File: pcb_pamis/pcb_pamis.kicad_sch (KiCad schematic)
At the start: 8 parts, among them J1 1755736, J2 USB_A, SW1 SW_Push, U1 ESP32-WROOM-32UE

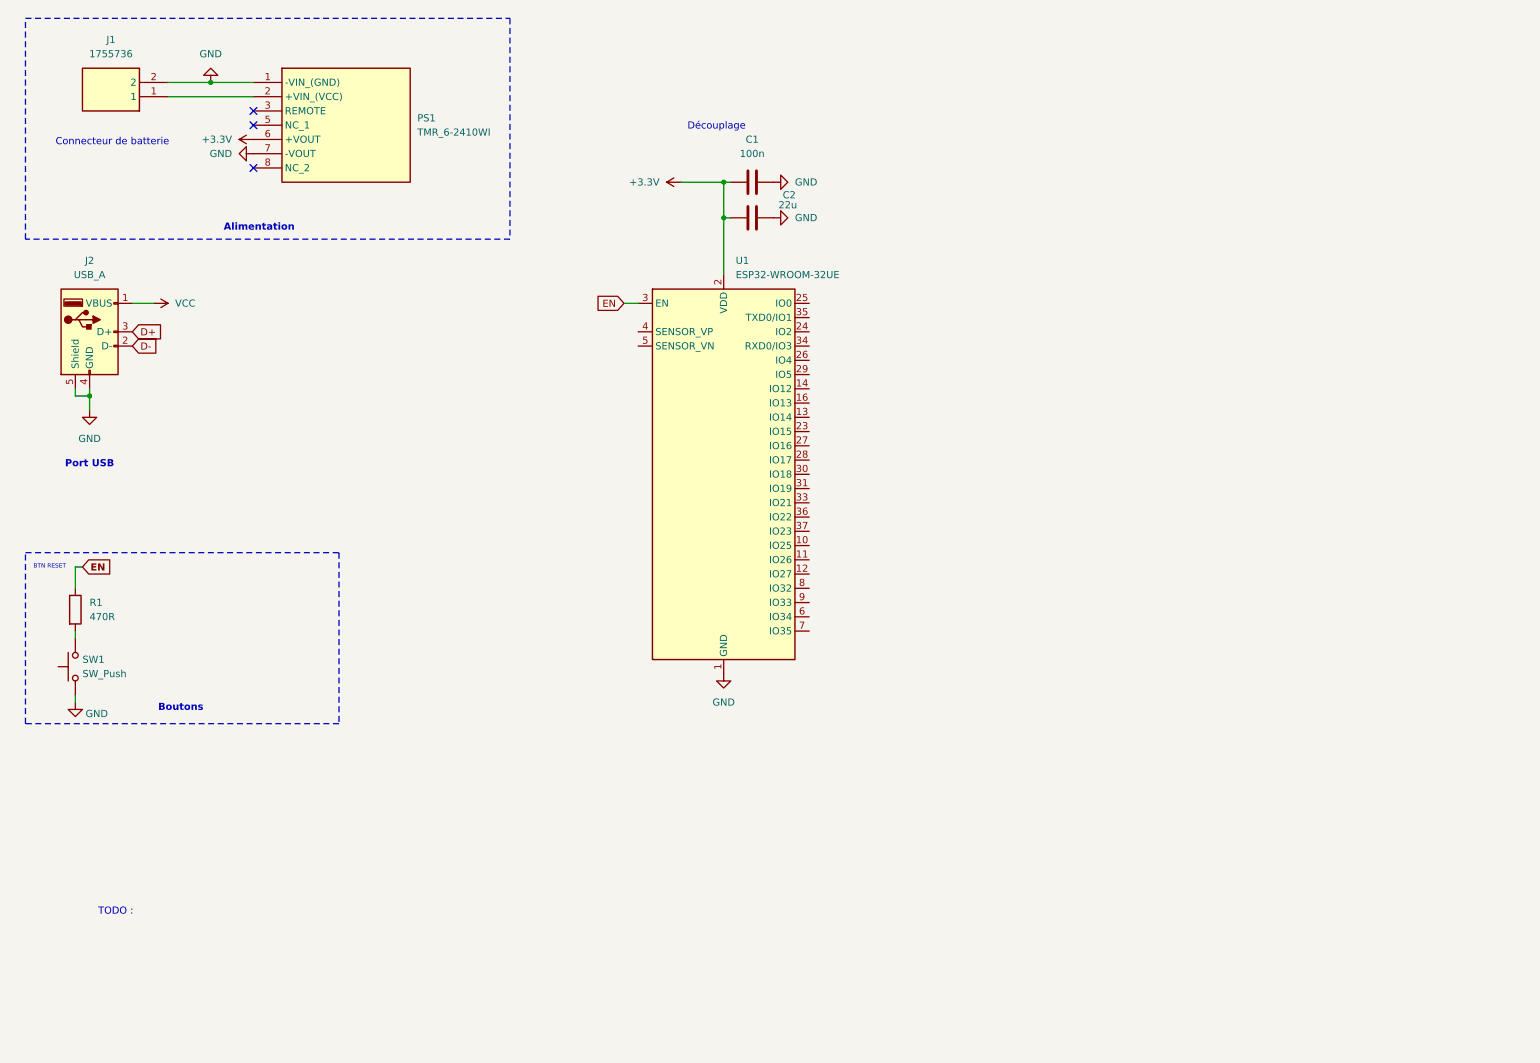
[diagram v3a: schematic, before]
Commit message: feat: add cp2102 usb to uart + auto flash circuit
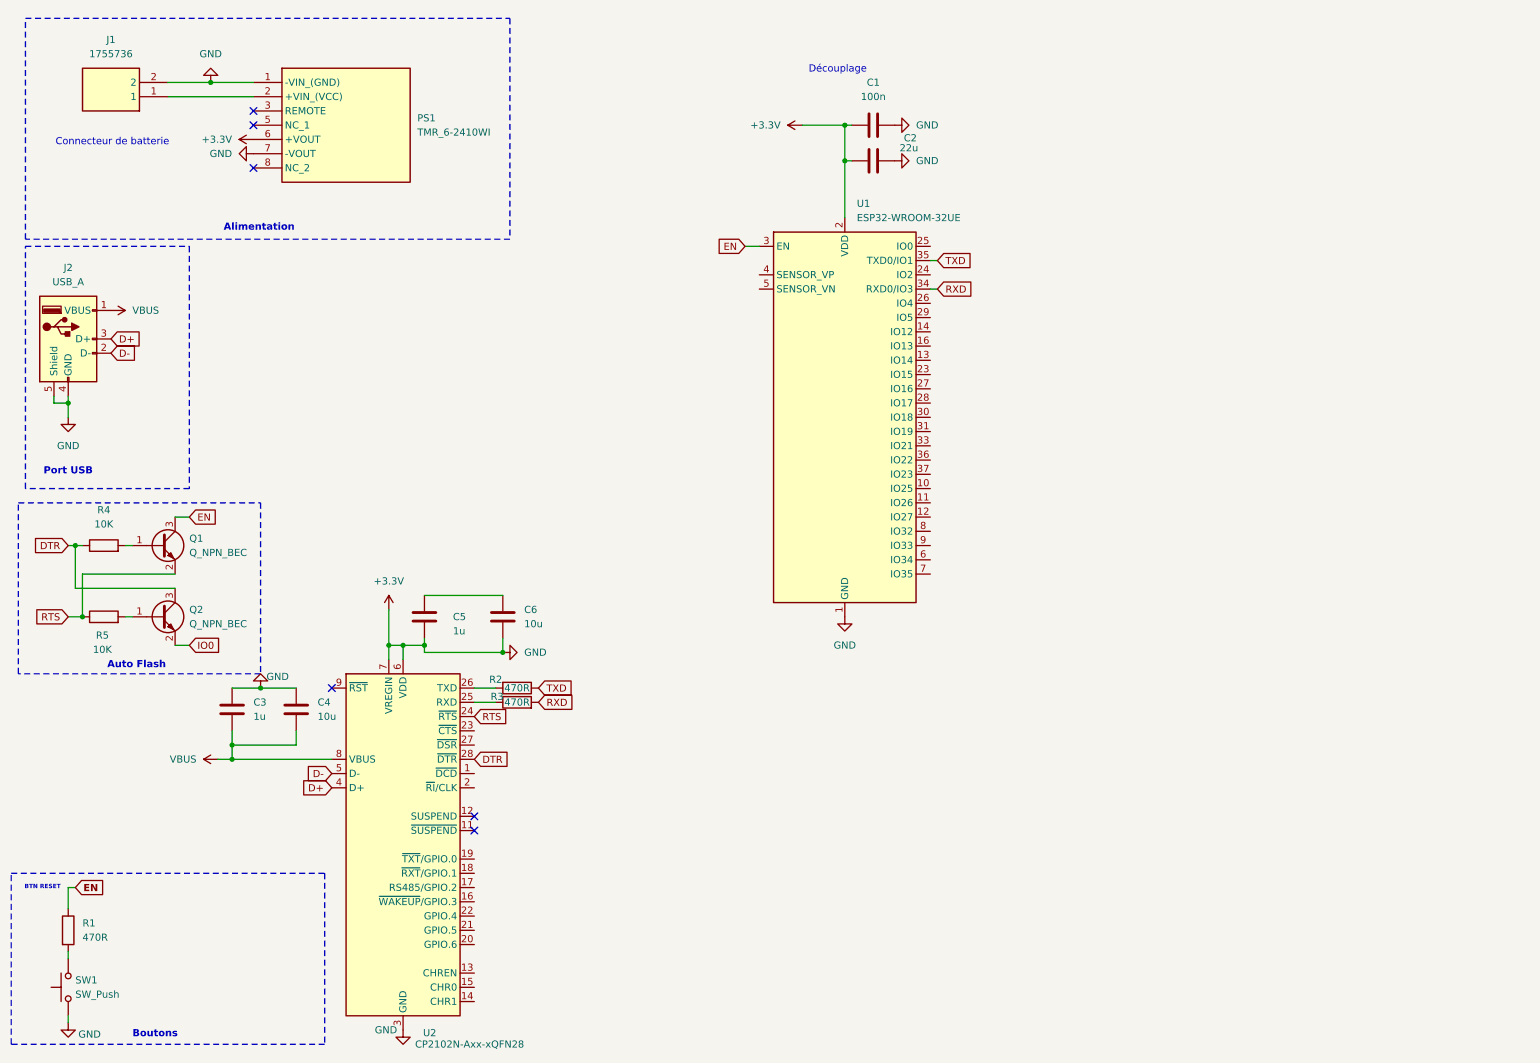
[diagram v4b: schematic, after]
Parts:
- added C3, C5: 1u, Capacitor_SMD:C_0805_2012Metric_Pad1.18x1.45mm_HandSolder, symbol Device:C
- added C4, C6: 10u, Capacitor_SMD:C_0805_2012Metric_Pad1.18x1.45mm_HandSolder, symbol Device:C
- added Q1, Q2: Q_NPN_BEC, symbol Transistor_BJT:Q_NPN_BEC
- added R2, R3: 470R, symbol Device:R
- added R4, R5: 10K, symbol Device:R
- added U2: CP2102N-Axx-xQFN28, Package_DFN_QFN:QFN-28-1EP_5x5mm_P0.5mm_EP3.35x3.35mm, symbol Interface_USB:CP2102N-Axx-xQFN28
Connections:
- net GND is gone; now on net +3.3V: C1.2, C2.2, J1.2, J2.4 (GND), J2.5 (Shield), PS1.1 (-VIN_(GND)), PS1.7 (-VOUT), SW1.1, U1.1 (GND), U1.15 (GND), U1.38 (GND), U1.39 (GND)
- net +3.3V: now also C3.2, C4.2, C5.1, C6.1, U2.29 (GND), U2.3 (GND), U2.6 (VDD), U2.7 (VREGIN)
- net D+: now also U2.4 (D+)
- net D-: now also U2.5 (D-)
- net EN: now also Q1.3 (C)
- net RXD: now reaches U1.34 (RXD0/IO3)
- net RXD: now also R3.2
- net TXD: now reaches U1.35 (TXD0/IO1)
- net TXD: now also R2.1
- net VCC renamed VBUS
- net VBUS: now also C3.1, C4.1, U2.8 (VBUS)
- new net: R2.2, U2.26 (TXD)
- new net: Q1.1 (B), R4.2
- new net: C5.2, C6.2
- new net: R3.1, U2.25 (RXD)
- new net: Q2.1 (B), R5.2
- new net DTR: Q2.3 (C), R4.1, U2.28 (~{DTR})
- new net IO0: Q2.2 (E)
- new net RTS: Q1.2 (E), R5.1, U2.24 (~{RTS})
- no-connect marks 3 -> 6
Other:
- note added: "Auto Flash"
- note removed: "TODO :"
- moved on the sheet: C1, C2, J2, R1, SW1, U1

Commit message: feat: cp2102 usb to uart
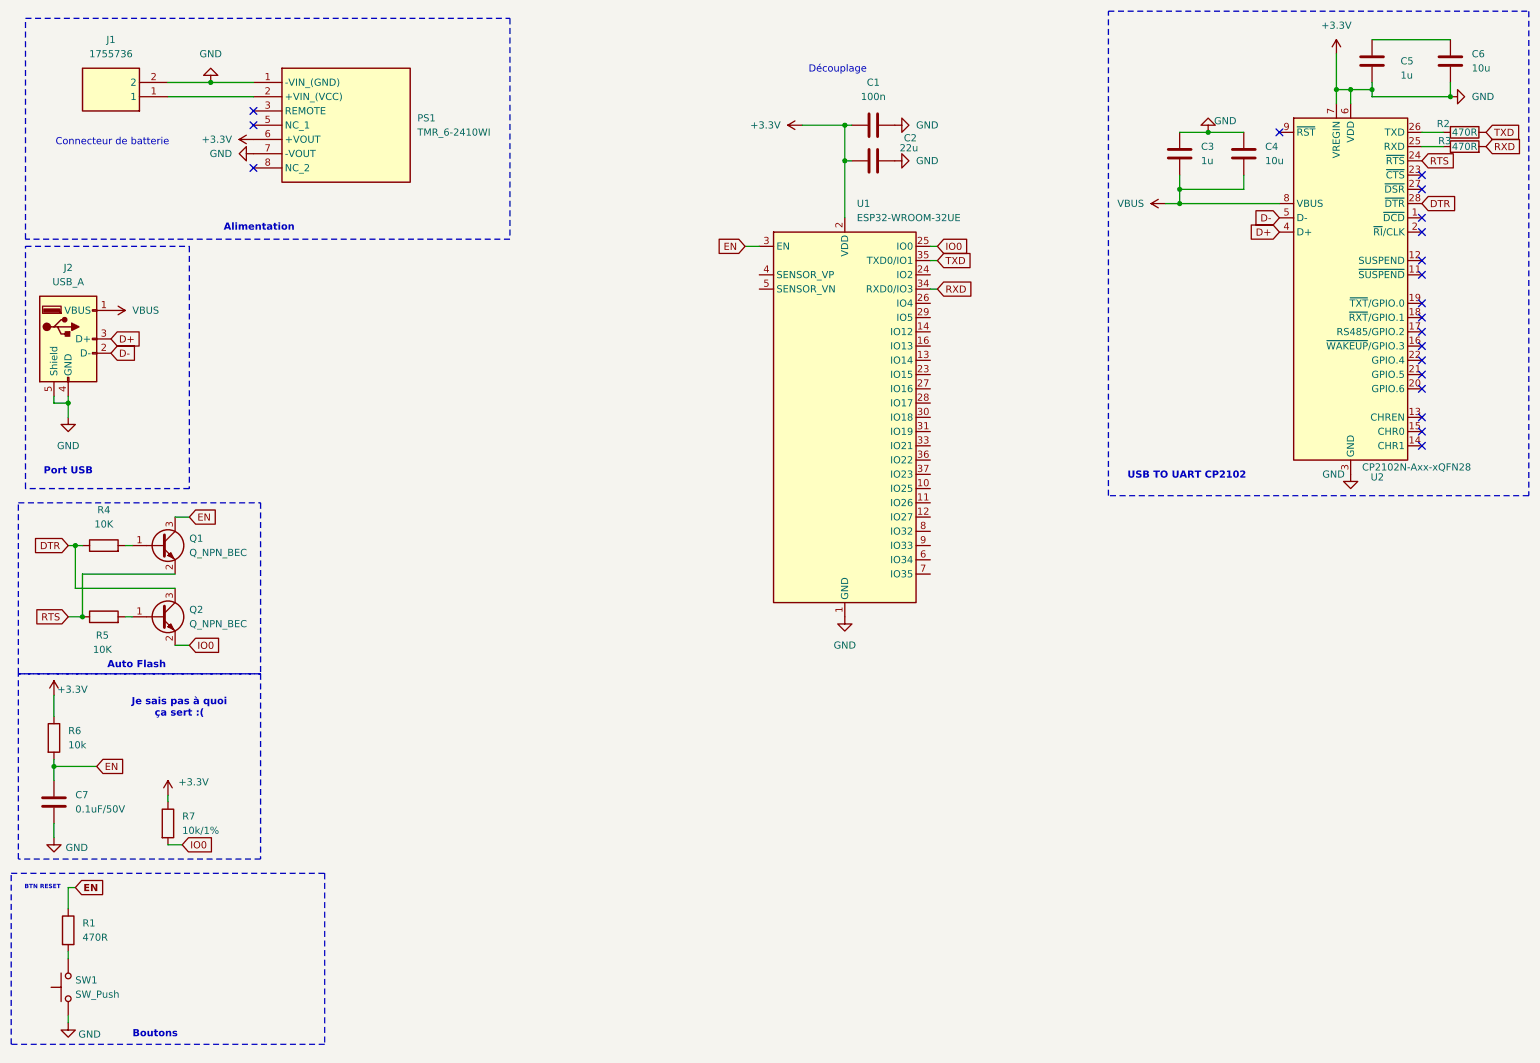
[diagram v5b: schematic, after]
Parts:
- added C7: 0.1uF/50V, Capacitor_SMD:C_0805_2012Metric_Pad1.18x1.45mm_HandSolder, symbol Device:C
- added R6: 10k, symbol Device:R
- added R7: 10k/1%, symbol Device:R
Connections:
- net +3.3V: now also C7.2, R6.1, R7.1
- net EN: now also C7.1, R6.2
- net IO0: now also U1.25 (IO0), R7.2
- no-connect marks 6 -> 20
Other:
- note added: "Je sais pas à quoi ça sert :("
- note added: "USB TO UART CP2102"
- moved on the sheet: C3, C4, C5, C6, R2, R3, U2

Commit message: correction alim PAMI et travail odo (WIP)
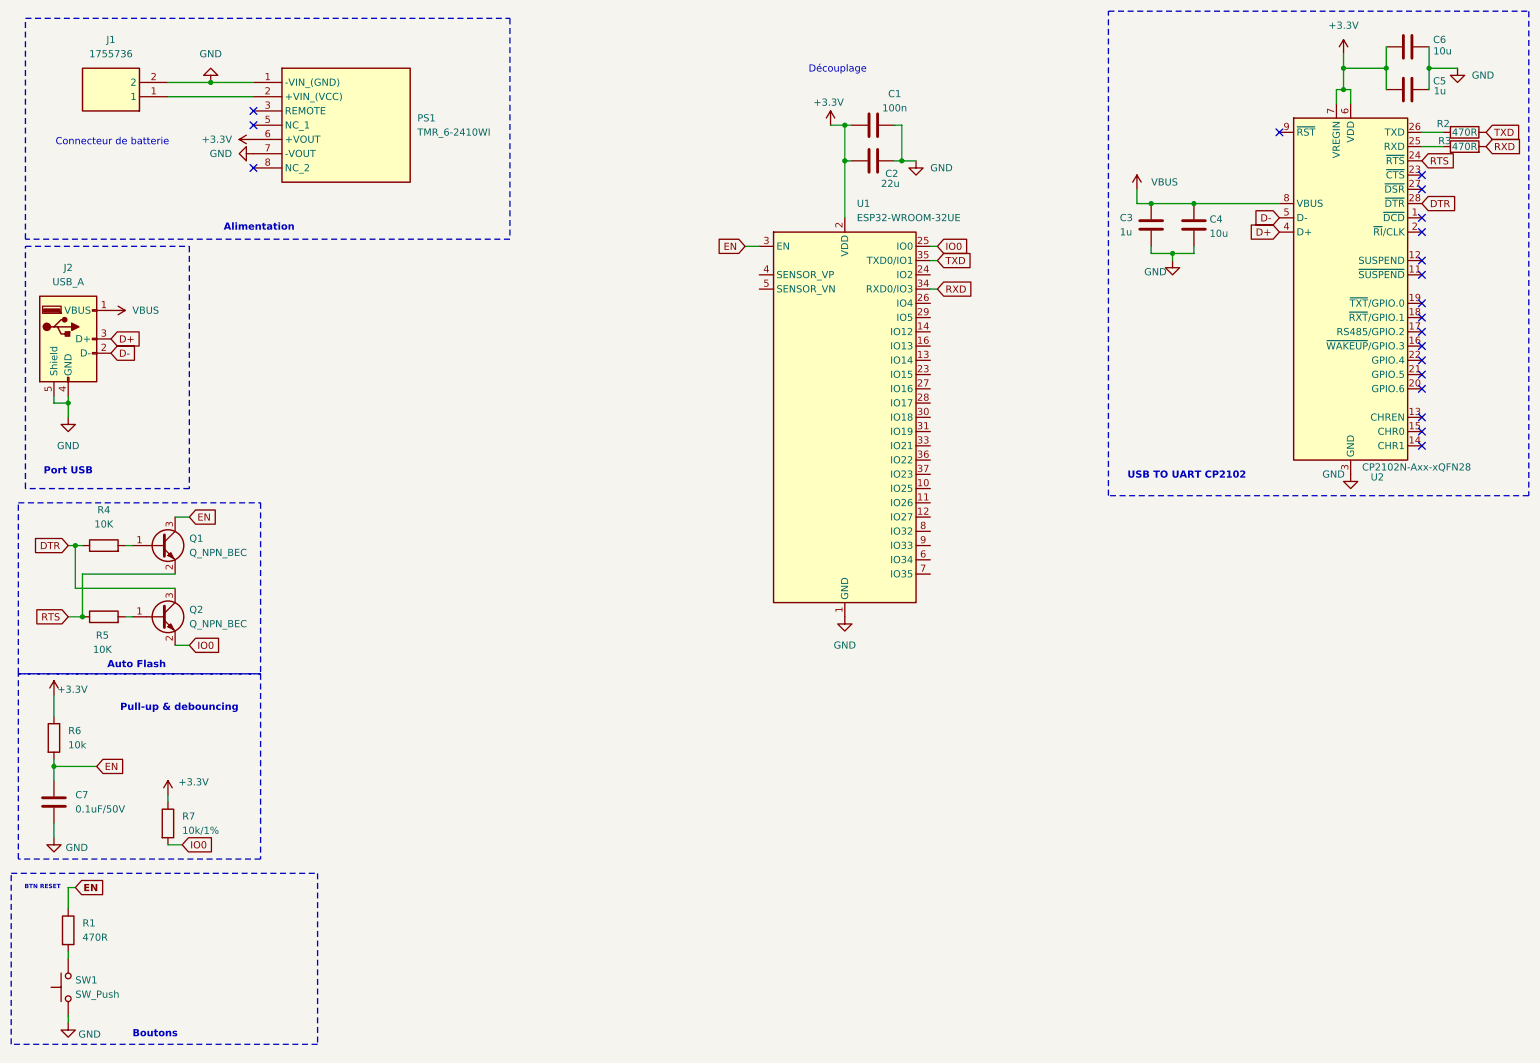
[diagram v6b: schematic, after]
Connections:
- net +3.3V: now also C5.2, C6.2; no longer C1.2, C2.2, C3.2, C4.2, C5.1, C6.1, C7.2, J1.2, J2.4 (GND), J2.5 (Shield), PS1.1 (-VIN_(GND)), PS1.7 (-VOUT), SW1.1, U1.1 (GND), U1.15 (GND), U1.38 (GND), U1.39 (GND), U2.29 (GND), U2.3 (GND)
- net VBUS: now also C3.2, C4.2; no longer C3.1, C4.1
- new net GND: C1.2, C2.2, C3.1, C4.1, C5.1, C6.1, C7.2, J1.2, J2.4 (GND), J2.5 (Shield), PS1.1 (-VIN_(GND)), PS1.7 (-VOUT), SW1.1, U1.1 (GND), U1.15 (GND), U1.38 (GND), U1.39 (GND), U2.29 (GND), U2.3 (GND)
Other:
- note added: "Pull-up & debouncing"
- note removed: "Je sais pas à quoi ça sert :("
- moved on the sheet: C3, C4, C5, C6

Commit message: ajout TMC2209
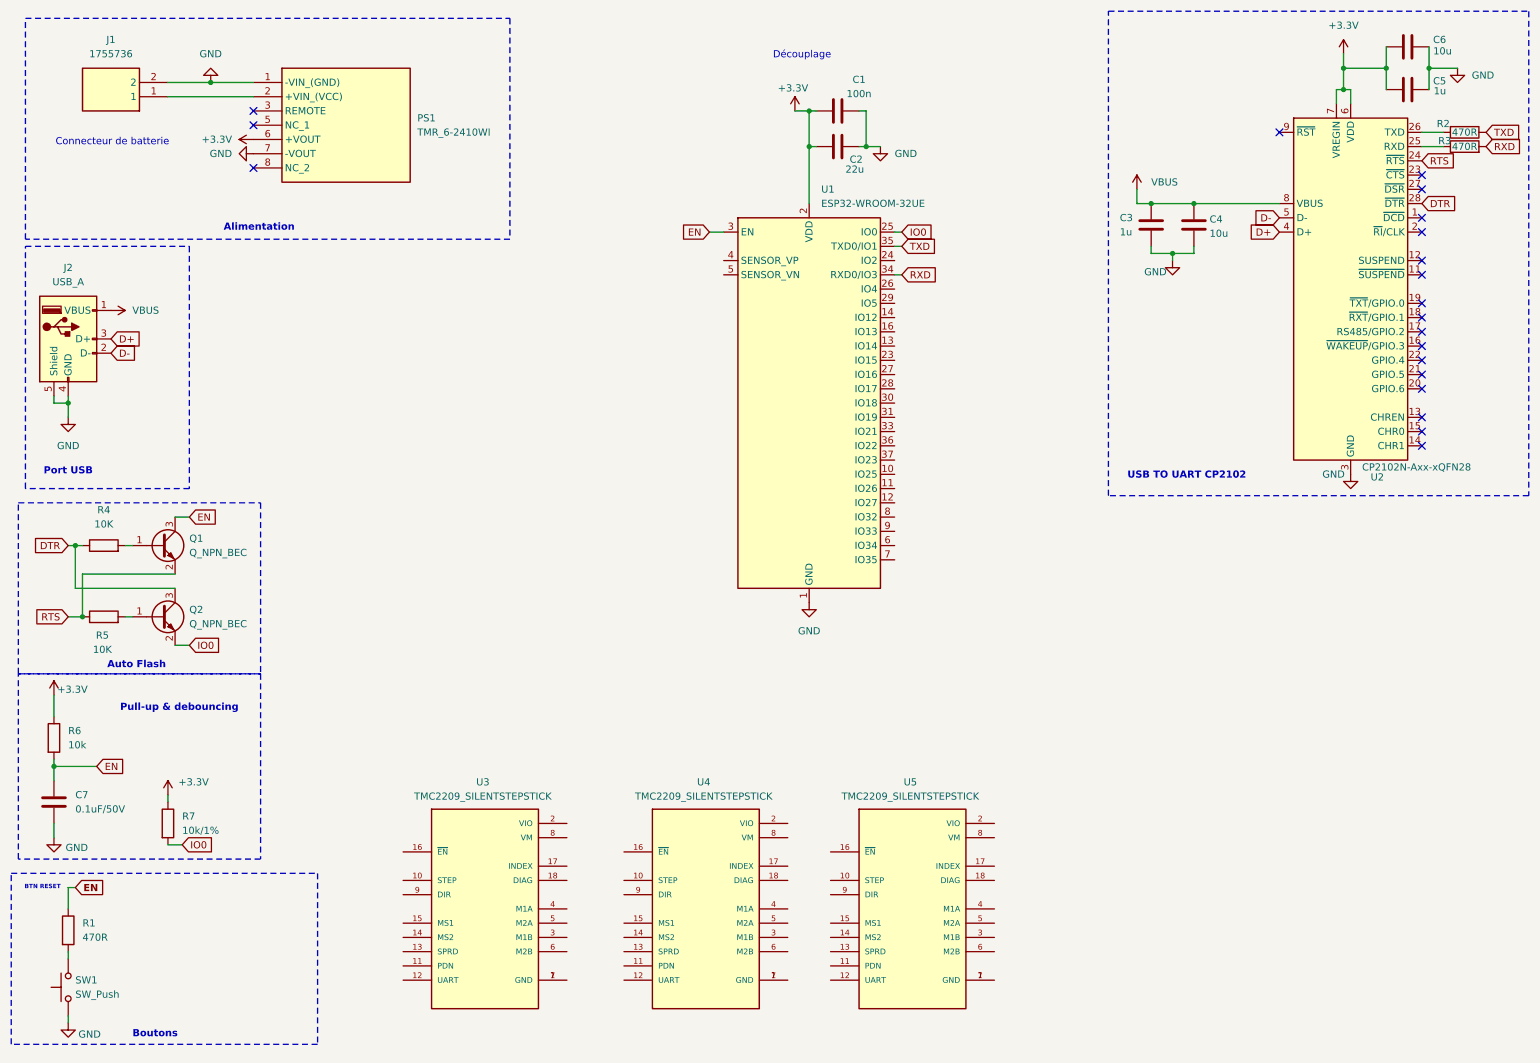
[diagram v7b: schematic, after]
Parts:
- added U3, U4, U5: TMC2209_SILENTSTEPSTICK, TMC2209_SILENTSTEPSTICK:MODULE_TMC2209_SILENTSTEPSTICK, symbol Modelec:TMC2209_SILENTSTEPSTICK
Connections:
- new net: U5.1 (GND), U5.7 (GND)
- new net: U4.1 (GND), U4.7 (GND)
- new net: U3.1 (GND), U3.7 (GND)
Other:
- moved on the sheet: C1, C2, U1

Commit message: drivers moteurs pap pamis
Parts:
- removed U3, U4, U5: TMC2209_SILENTSTEPSTICK, TMC2209_SILENTSTEPSTICK:MODULE_TMC2209_SILENTSTEPSTICK, symbol Modelec:TMC2209_SILENTSTEPSTICK
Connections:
- net VCC: now reaches J1.1, PS1.2 (+VIN_(VCC))
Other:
- added sheet Drivers moteurs pas à pas (drv_moteurs_pap.kicad_sch)
